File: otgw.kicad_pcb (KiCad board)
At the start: 2 copper layers, 92 x 60 mm, 44 parts, among them CON1 BARREL_JACK, P2 CONN_01X05, P3 CONN_01X03, P4 CONN_01X02, P5 CONN_01X02, P6 MYSX_2.0, P7 CONN_01X06, Q1 BC558, Q2 BC558, Q3 BC558, Q4 BC547, Q5 BC558, U1 PIC16(L)F88-I/P, U2 PC827, U3 7805

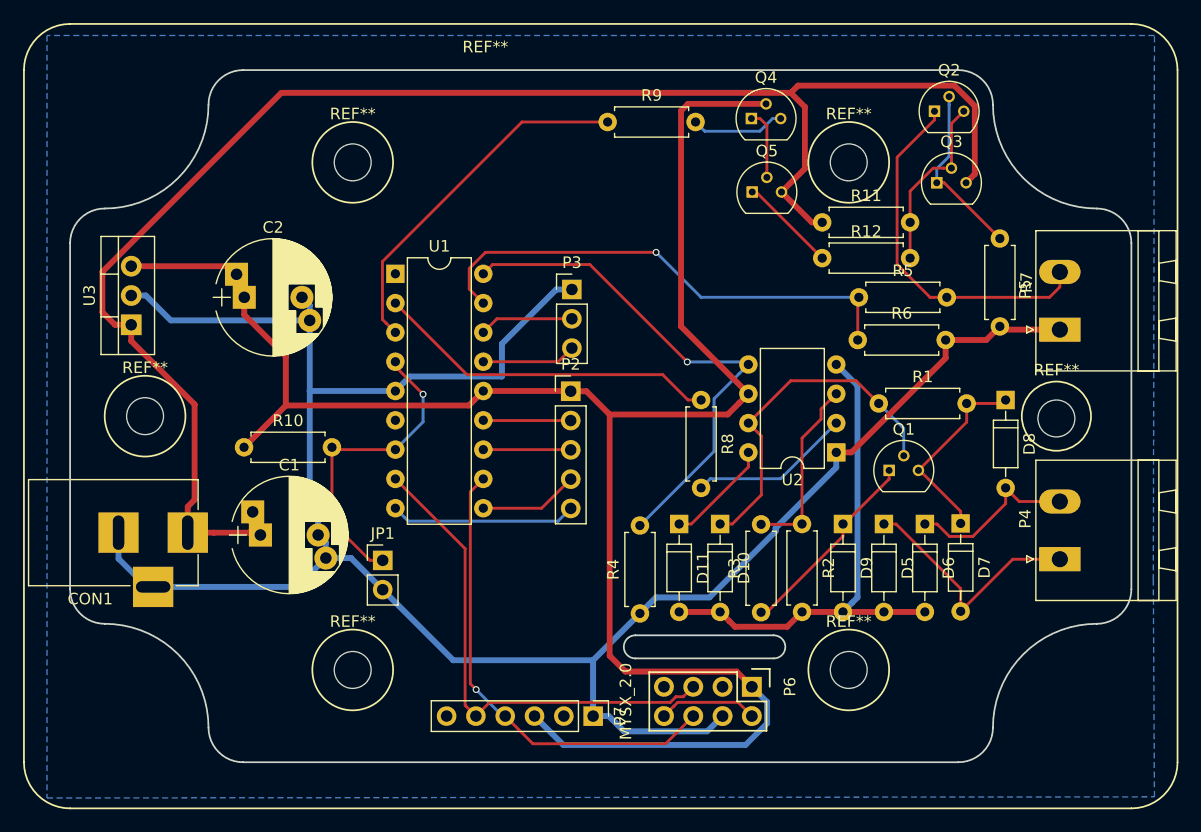
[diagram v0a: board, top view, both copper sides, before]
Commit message: Fixed the silk screen
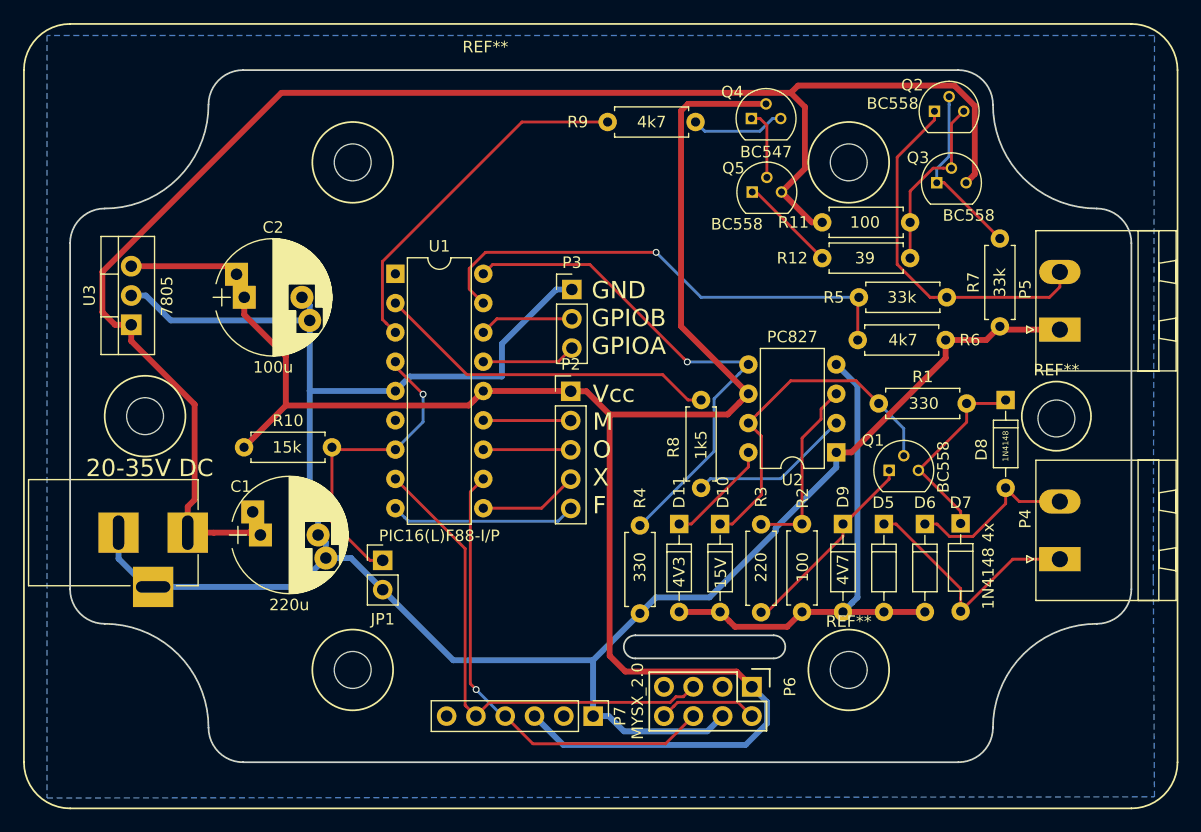
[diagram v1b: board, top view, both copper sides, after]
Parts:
- added G***: LOGO, Open_Hardware:Full_OSHW_scaled, B.Cu at (79.0, 96.8)
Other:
- board text added: "1N4148 4x"
- board text added: "20-35V DC"
- board text added: "GND GPIOB GPIOA"
- board text added: "Vcc M O X F"
- board text added: "mysensors opentherm gateway Rev 0 https://github.com/dirkjankrijnders/mysensors-opentherm Original gateway: http://otgw.tclcode.com"

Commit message: Annotations on the schematic and some small Silkscreen additions
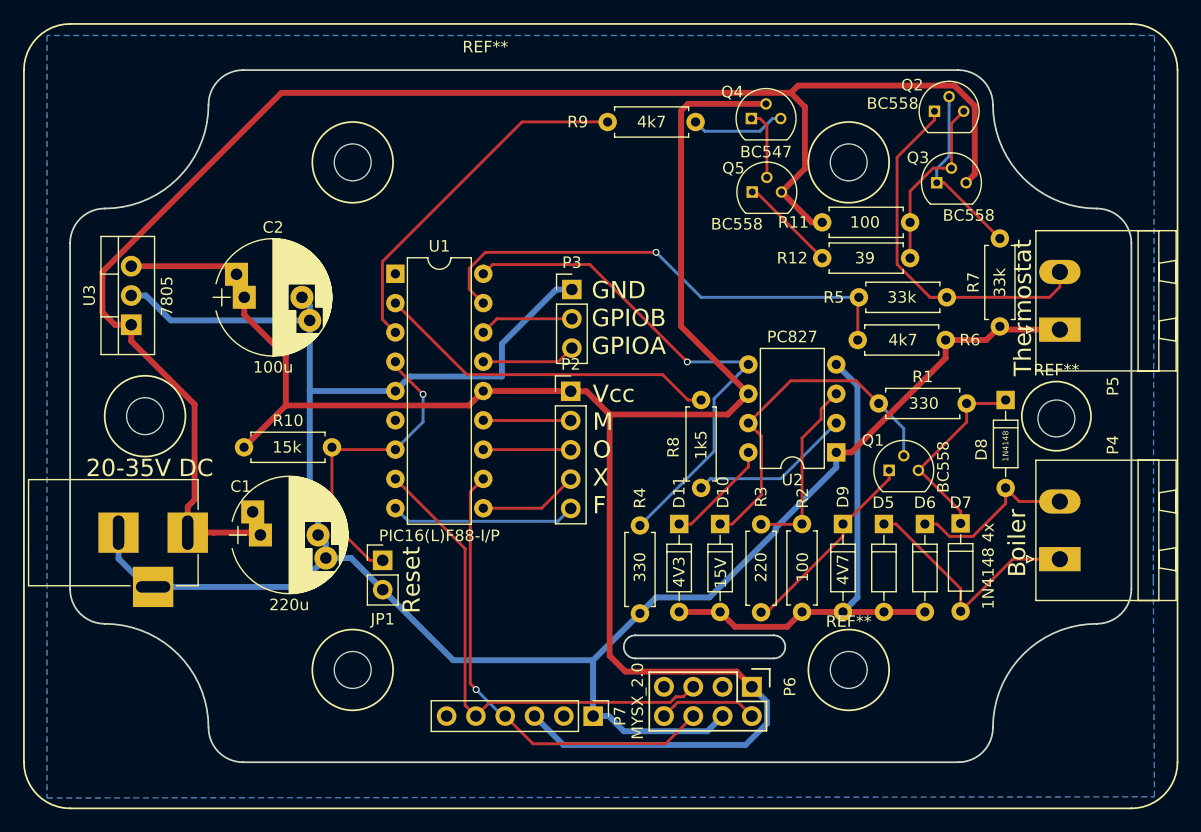
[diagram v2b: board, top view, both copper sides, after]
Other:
- board text added: "Boiler"
- board text added: "Reset"
- board text added: "Thermostat"
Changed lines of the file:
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@@
     (links 0)
     (no_connects 0)
-    (area 87.924999 98.924999 102.075001 101.075001)
+    (area 35.721799 45.721799 137.8782 114.278201)
     (thickness 1.6)
-    (drawings 9)
+    (drawings 12)
     (tracks 275)
     (zones 0)
@@
     (descr "Generic Phoenix Contact connector footprint for series: MSTBA-G; number of pins: 02; pin pitch: 5.00mm; Angled || order number: 1923759 16A (HC) || order number: 1757475 12A")
     (tags "phoenix_contact connector MSTBA_01x02_G_5.00mm")
-    (fp_text reference P4 (at 3.5 -3 90) (layer F.SilkS)
+    (fp_text reference P4 (at 9.9 4.6 90) (layer F.SilkS)
       (effects (font (size 1 1) (thickness 0.15)))
     )
@@
     (descr "Generic Phoenix Contact connector footprint for series: MSTBA-G; number of pins: 02; pin pitch: 5.00mm; Angled || order number: 1923759 16A (HC) || order number: 1757475 12A")
     (tags "phoenix_contact connector MSTBA_01x02_G_5.00mm")
-    (fp_text reference P5 (at 3.5 -3 90) (layer F.SilkS)
+    (fp_text reference P5 (at -4.9 4.6 90) (layer F.SilkS)
       (effects (font (size 1 1) (thickness 0.15)))
     )
@@
       (xy 3.189172 5.565124) (xy 3.297425 5.576049) (xy 3.323167 5.572722)) (layer B.SilkS) (width 0.003))
   )
+  (gr_text Reset (at 69.6 94.2 90) (layer F.SilkS)
+    (effects (font (size 1.5 1.5) (thickness 0.3)))
+  )
+  (gr_text Thermostat (at 122.6 70.6 90) (layer F.SilkS)
+    (effects (font (size 1.5 1.5) (thickness 0.3)))
+  )
+  (gr_text Boiler (at 122.1 91 90) (layer F.SilkS)
+    (effects (font (size 1.5 1.5) (thickness 0.3)))
+  )
   (gr_text "mysensors opentherm gateway Rev 0\nhttps://github.com/dirkjankrijnders/mysensors-opentherm\nOriginal gateway: http://otgw.tclcode.com" (at 96.5 62.4) (layer B.SilkS)

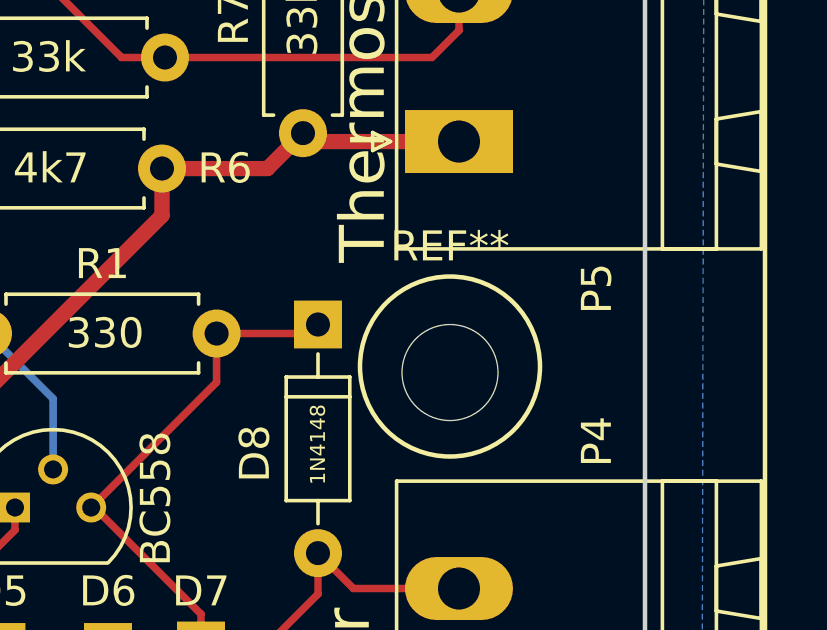
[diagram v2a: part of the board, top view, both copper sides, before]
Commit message: Centered a mounting hole
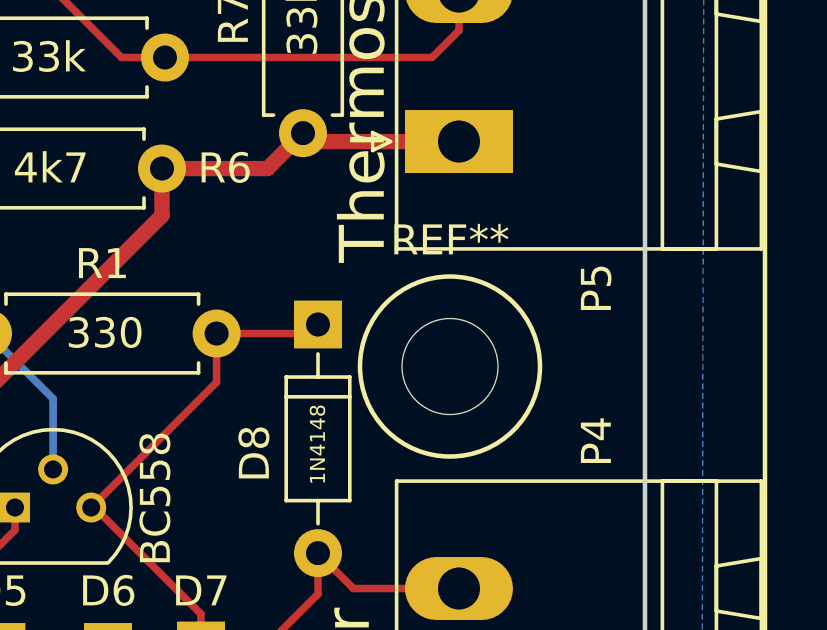
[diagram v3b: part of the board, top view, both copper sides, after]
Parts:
- moved REF** 0.20 mm to (125.5, 80.0)
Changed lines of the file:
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@@
 (kicad_pcb (version 4) (host pcbnew 4.0.5)
   (general
-    (links 0)
+    (links 83)
     (no_connects 0)
     (area 35.721799 45.721799 137.8782 114.278201)
@@
   )
   (module Mounting_Holes:MountingHole_3.2mm_M3 (layer F.Cu)
-    (at 125.5 80.2)
+    (at 125.5 80)
     (descr "Mounting Hole 3.2mm, no annular, M3")
     (tags "mounting hole 3.2mm no annular m3")
